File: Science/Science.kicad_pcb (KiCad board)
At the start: 2 copper layers, 58.3 x 70.8 mm, 5 parts, among them J1 Screw_Terminal_01x12, J2 Screw_Terminal_01x12, U1 LM1084-5.0

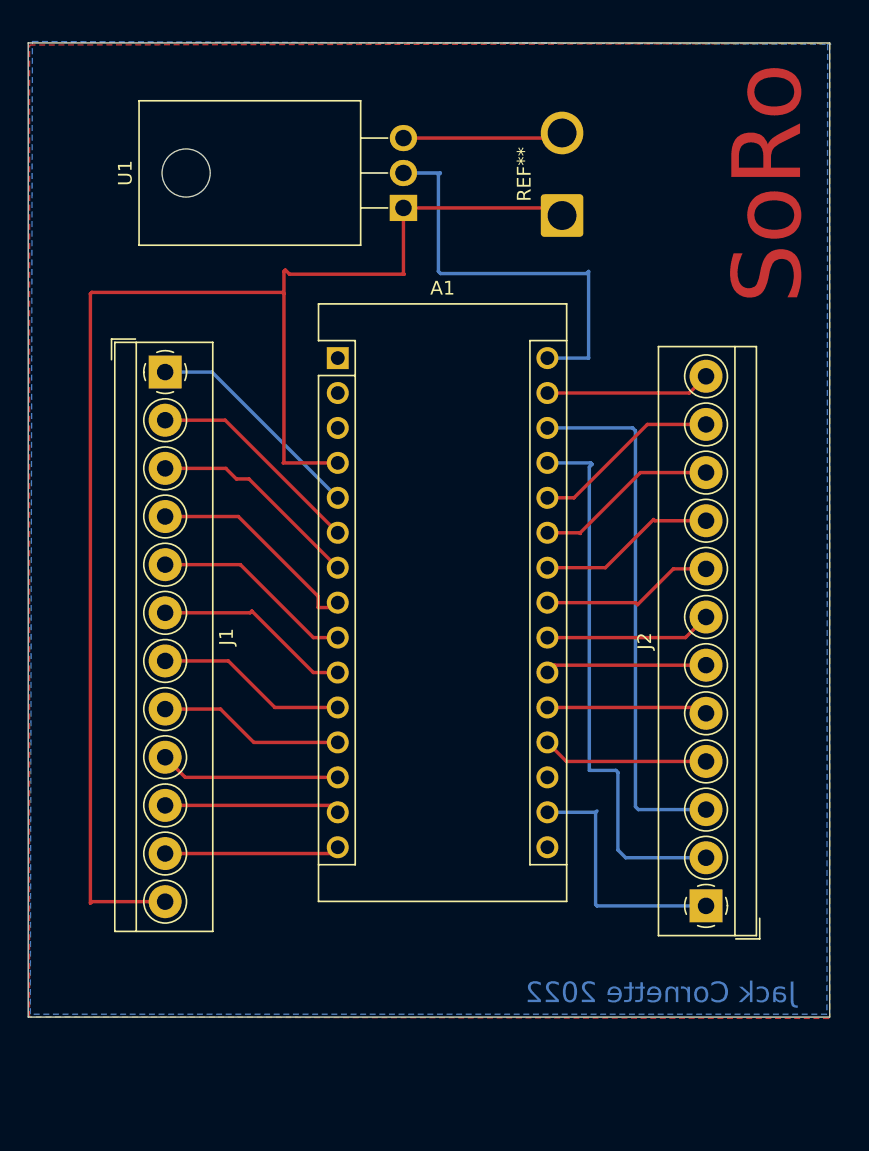
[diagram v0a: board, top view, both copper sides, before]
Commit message: Updated Arduino README.. still needs more
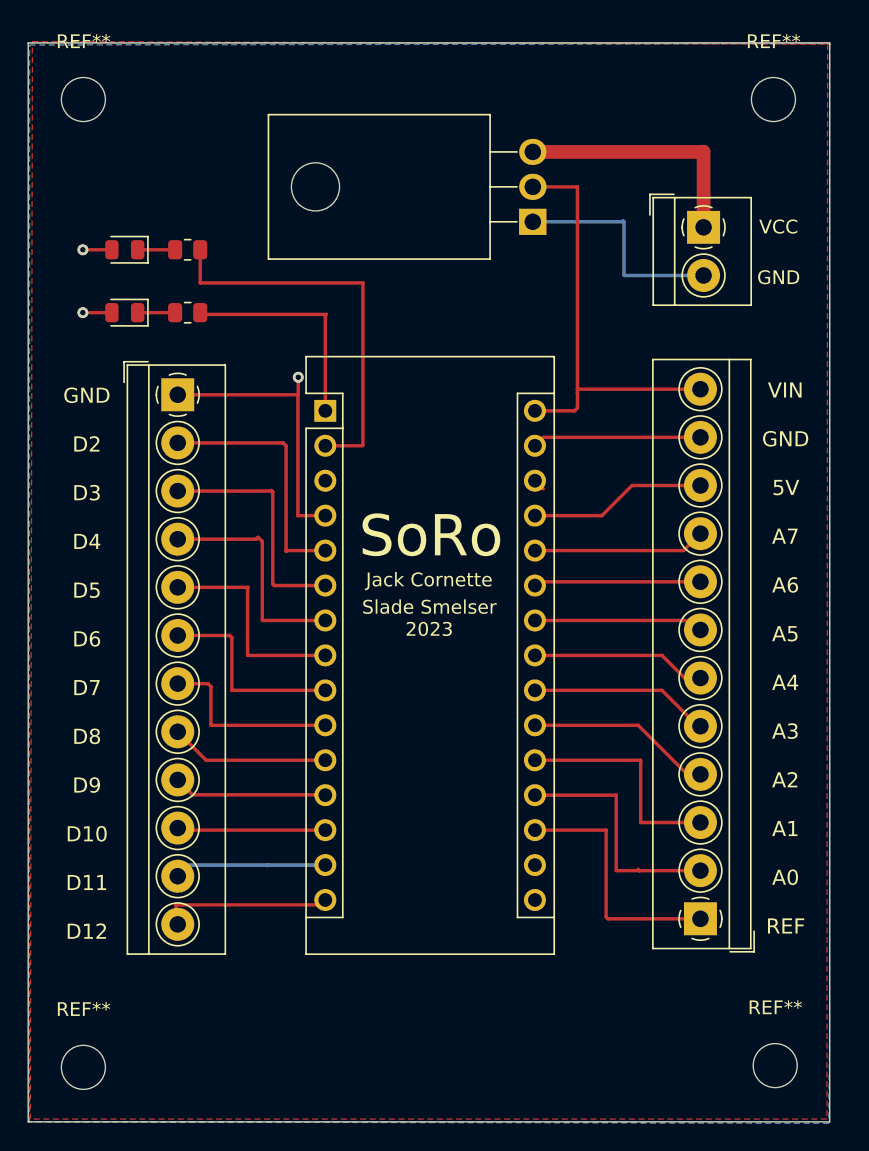
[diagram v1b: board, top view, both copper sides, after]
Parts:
- removed the REF** at (140.5, 68.4)
- added CAN: LED_0805_2012Metric, LED_SMD:LED_0805_2012Metric, F.Cu at (108.7, 70.9)
- added J3: Screw_Terminal_01x02, TerminalBlock_4Ucon:TerminalBlock_4Ucon_1x02_P3.50mm_Horizontal, F.Cu at (150.7, 69.2)
- added R3: R_US, Resistor_SMD:R_0805_2012Metric, F.Cu at (113.2, 70.9)
- added R3: R_US, Resistor_SMD:R_0805_2012Metric, F.Cu at (113.2, 75.4)
- added REF**: LED_0805_2012Metric, LED_SMD:LED_0805_2012Metric, F.Cu at (108.7, 75.4)
- added REF**: MountingHole_3.2mm_M3, MountingHole:MountingHole_3.2mm_M3, F.Cu at (156.0, 130.2)
- added REF**: MountingHole_3.2mm_M3, MountingHole:MountingHole_3.2mm_M3, F.Cu at (105.7, 59.9)
- added REF**: MountingHole_3.2mm_M3, MountingHole:MountingHole_3.2mm_M3, F.Cu at (155.8, 59.9)
- added REF**: MountingHole_3.2mm_M3, MountingHole:MountingHole_3.2mm_M3, F.Cu at (105.7, 130.3)
- moved U1 9.46 mm to (138.3, 68.8)
- moved A1 3.94 mm to (123.3, 82.6)
- moved J1 1.89 mm to (112.5, 81.4)
- moved J2 1.02 mm to (150.5, 119.5)
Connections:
- A1 pad 1: unconnected-(A1-Pad1) -> (no net)
- A1 pad 10: Net-(A1-Pad10) -> (no net)
- A1 pad 11: Net-(A1-Pad11) -> (no net)
- A1 pad 14: Net-(A1-Pad14) -> (no net)
- A1 pad 16: unconnected-(A1-Pad16) -> (no net)
- A1 pad 2: unconnected-(A1-Pad2) -> (no net)
- A1 pad 5: Net-(A1-Pad5) -> (no net)
- J1 pad 1: Net-(A1-Pad5) -> GND
- J1 pad 10: Net-(A1-Pad14) -> Net-(A1-Pad13)
- J1 pad 11: Net-(A1-Pad15) -> (no net)
- J1 pad 12: GND -> Net-(A1-Pad15)
- J1 pad 2: Net-(A1-Pad6) -> (no net)
- J1 pad 3: Net-(A1-Pad7) -> Net-(A1-Pad6)
- J1 pad 4: Net-(A1-Pad8) -> Net-(A1-Pad7)
- J1 pad 5: Net-(A1-Pad9) -> Net-(A1-Pad8)
- J1 pad 6: Net-(A1-Pad10) -> Net-(A1-Pad9)
- J1 pad 7: Net-(A1-Pad11) -> (no net)
- J1 pad 8: Net-(A1-Pad12) -> (no net)
- J1 pad 9: Net-(A1-Pad13) -> Net-(A1-Pad12)
- J2 pad 1: Net-(A1-Pad17) -> unconnected-(A1-Pad18)
- J2 pad 10: Net-(A1-Pad25) -> Net-(A1-Pad27)
- J2 pad 11: Net-(A1-Pad26) -> Net-(A1-Pad29)
- J2 pad 12: Net-(A1-Pad29) -> Net-(A1-Pad30)
- J2 pad 2: Net-(A1-Pad27) -> Net-(A1-Pad19)
- J2 pad 3: Net-(A1-Pad28) -> Net-(A1-Pad20)
- J2 pad 4: Net-(A1-Pad19) -> Net-(A1-Pad21)
- J2 pad 5: Net-(A1-Pad20) -> Net-(A1-Pad22)
- J2 pad 6: Net-(A1-Pad21) -> Net-(A1-Pad23)
- J2 pad 7: Net-(A1-Pad22) -> Net-(A1-Pad24)
- J2 pad 8: Net-(A1-Pad23) -> Net-(A1-Pad25)
- J2 pad 9: Net-(A1-Pad24) -> Net-(A1-Pad26)
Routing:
- net (no net): track 0.00 -> 106.5 mm
- net GND: track 107.3 -> 41.4 mm, vias 0 -> 3
- net Net-(A1-Pad28): track 39.0 -> 0.85 mm
- net Net-(A1-Pad27): track 40.0 -> 12.9 mm
- net Net-(A1-Pad17): track 18.4 -> 0.00 mm
- net unconnected-(A1-Pad18): track 0.00 -> 18.4 mm
- net Net-(A1-Pad5): track 16.3 -> 0.00 mm
- net Net-(A1-Pad10): track 14.5 -> 0.00 mm
- net Net-(A1-Pad11): track 13.9 -> 0.00 mm
- net Net-(A1-Pad14): track 12.8 -> 0.00 mm
- net +BATT: track 11.7 -> 18.0 mm
- net Net-(A1-Pad19): track 12.1 -> 18.3 mm
- net Net-(A1-Pad20): track 11.7 -> 16.5 mm
- net Net-(A1-Pad12): track 13.6 -> 11.2 mm
- net Net-(A1-Pad13): track 13.2 -> 10.8 mm
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- added copper zone on B.Cu, net GND
- added copper zone on F.Cu, net Net-(A1-Pad30)
- removed copper zone on F.Cu, net GND
- removed copper zone on B.Cu, net Net-(A1-Pad30)
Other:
- board size 58.3 x 70.8 mm -> 58.3 x 78.4 mm
- board text added: "GND"
- board text added: "GND D2 D3 D4 D5 D6 D7 D8 D9 D10 D11 D12"
- board text added: "Jack Cornette"
- board text added: "Slade Smelser 2023"
- board text added: "VCC"
- board text added: "VIN GND 5V A7 A6 A5 A4 A3 A2 A1 A0 REF"
- board text removed: "Jack Cornette 2022"
